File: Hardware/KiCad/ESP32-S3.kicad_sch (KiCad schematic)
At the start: 48 parts, among them J1 UJ20-C-H-G-SMT-1-P16-TR, J4 RJ45, J5 Conn_TagConnect_TC2030-NL_ESP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, U1 ESP32-S3-WROOM-1, U5 WE-TVS-82400102, U7 AP7333-33SRG-7

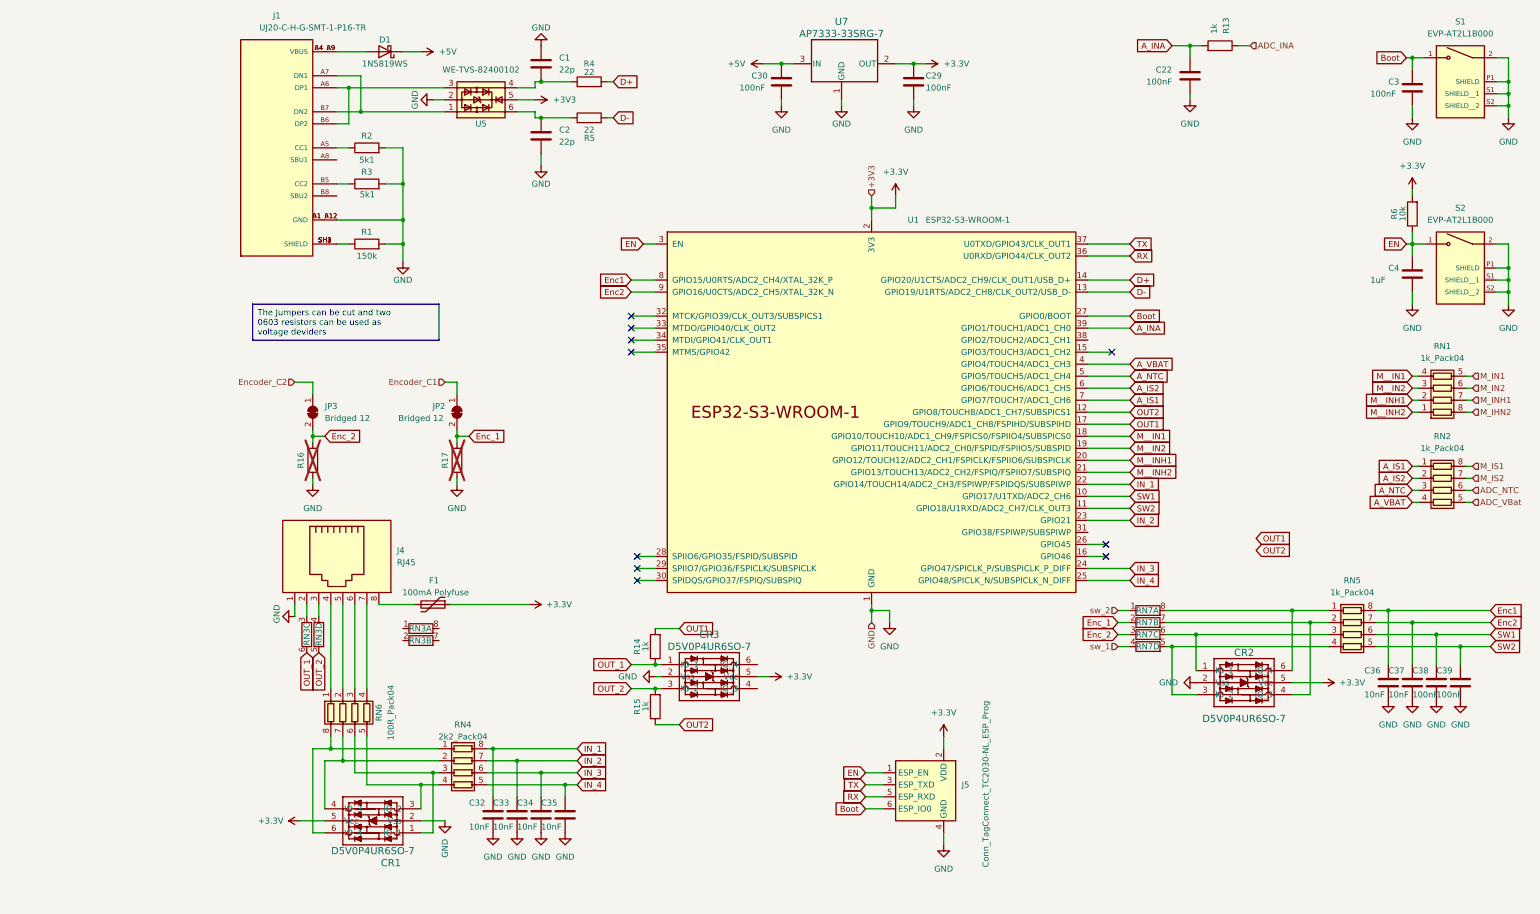
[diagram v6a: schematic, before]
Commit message: update PCB
Add voltage selector solder jumper vor rj45 connector to switch between 12V and 3.3V vor the control panel
Add voltage supression diodes for IS pins from the motor driver ICs
Fix DRC violations
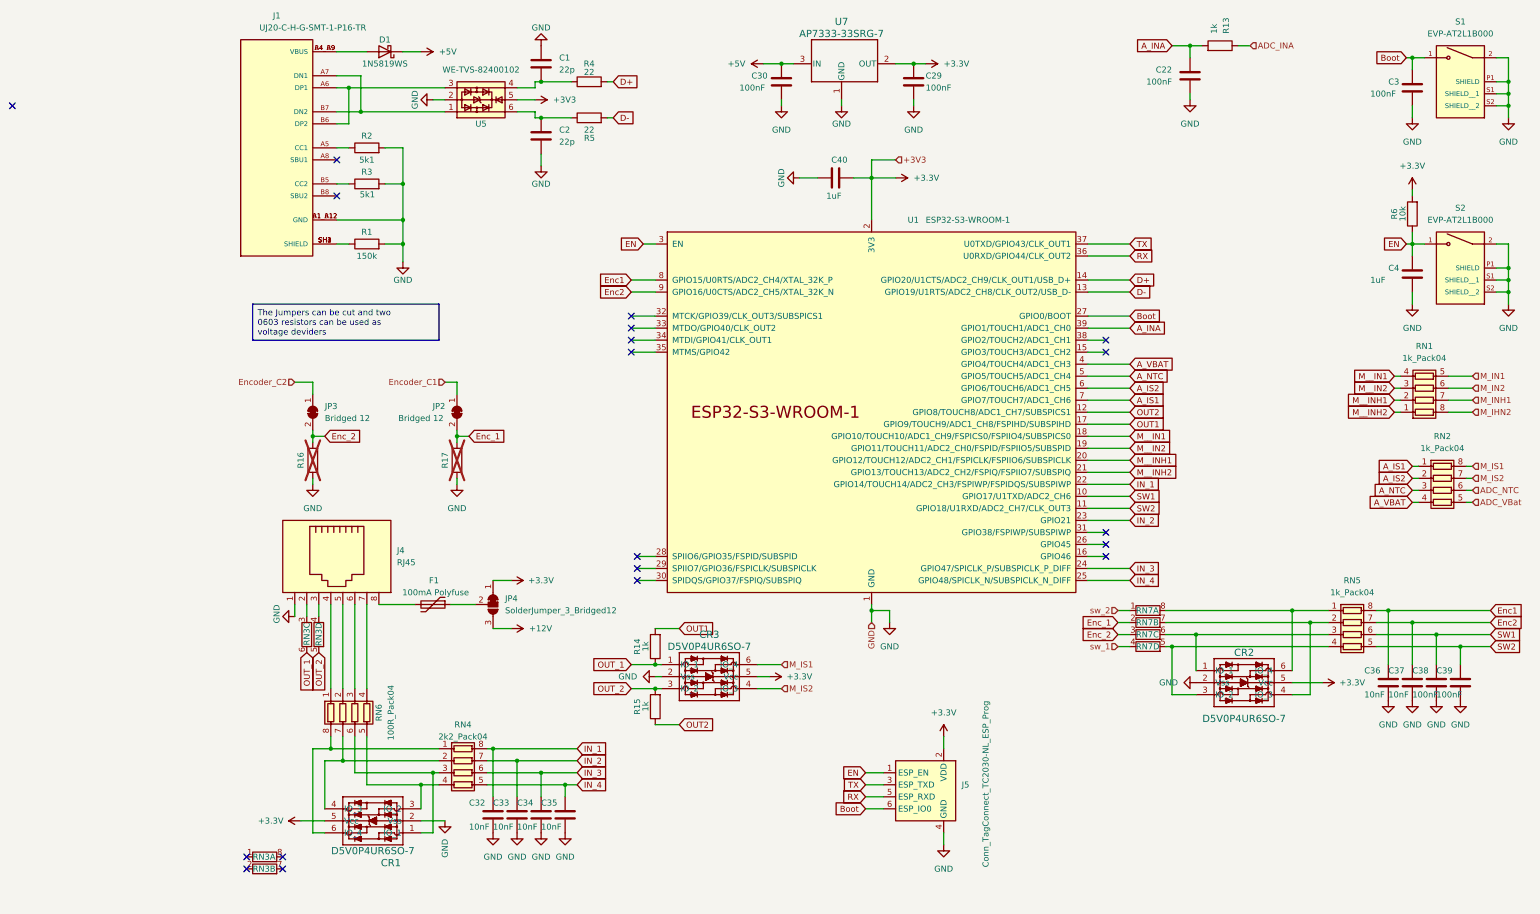
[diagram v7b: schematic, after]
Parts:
- added C40: 1uF, Capacitor_SMD:C_0603_1608Metric, symbol Device:C
- added JP4: SolderJumper_3_Bridged12, BugWiper_lib:SolderJumper_3P_R_SMD_0603_Bridged_12, symbol Jumper:SolderJumper_3_Bridged12
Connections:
- net +3.3V: now also C40.2, JP4.1 (A); no longer F1.1
- net GND: now also C40.1
- net M_IS1: now also CR3.6 (IO_4)
- net M_IS2: now also CR3.4 (IO_3)
- new net: F1.1, JP4.2 (C)
- new net +12V: JP4.3 (B)
- no-connect marks 10 -> 19
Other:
- moved on the sheet: RN1, RN3A, RN3B
